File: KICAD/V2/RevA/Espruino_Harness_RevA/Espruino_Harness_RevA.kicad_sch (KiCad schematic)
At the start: 2 parts, among them J900 TARGET INTERFACE CONNECTOR A, J901 TARGET INTERFACE CONNECTOR B

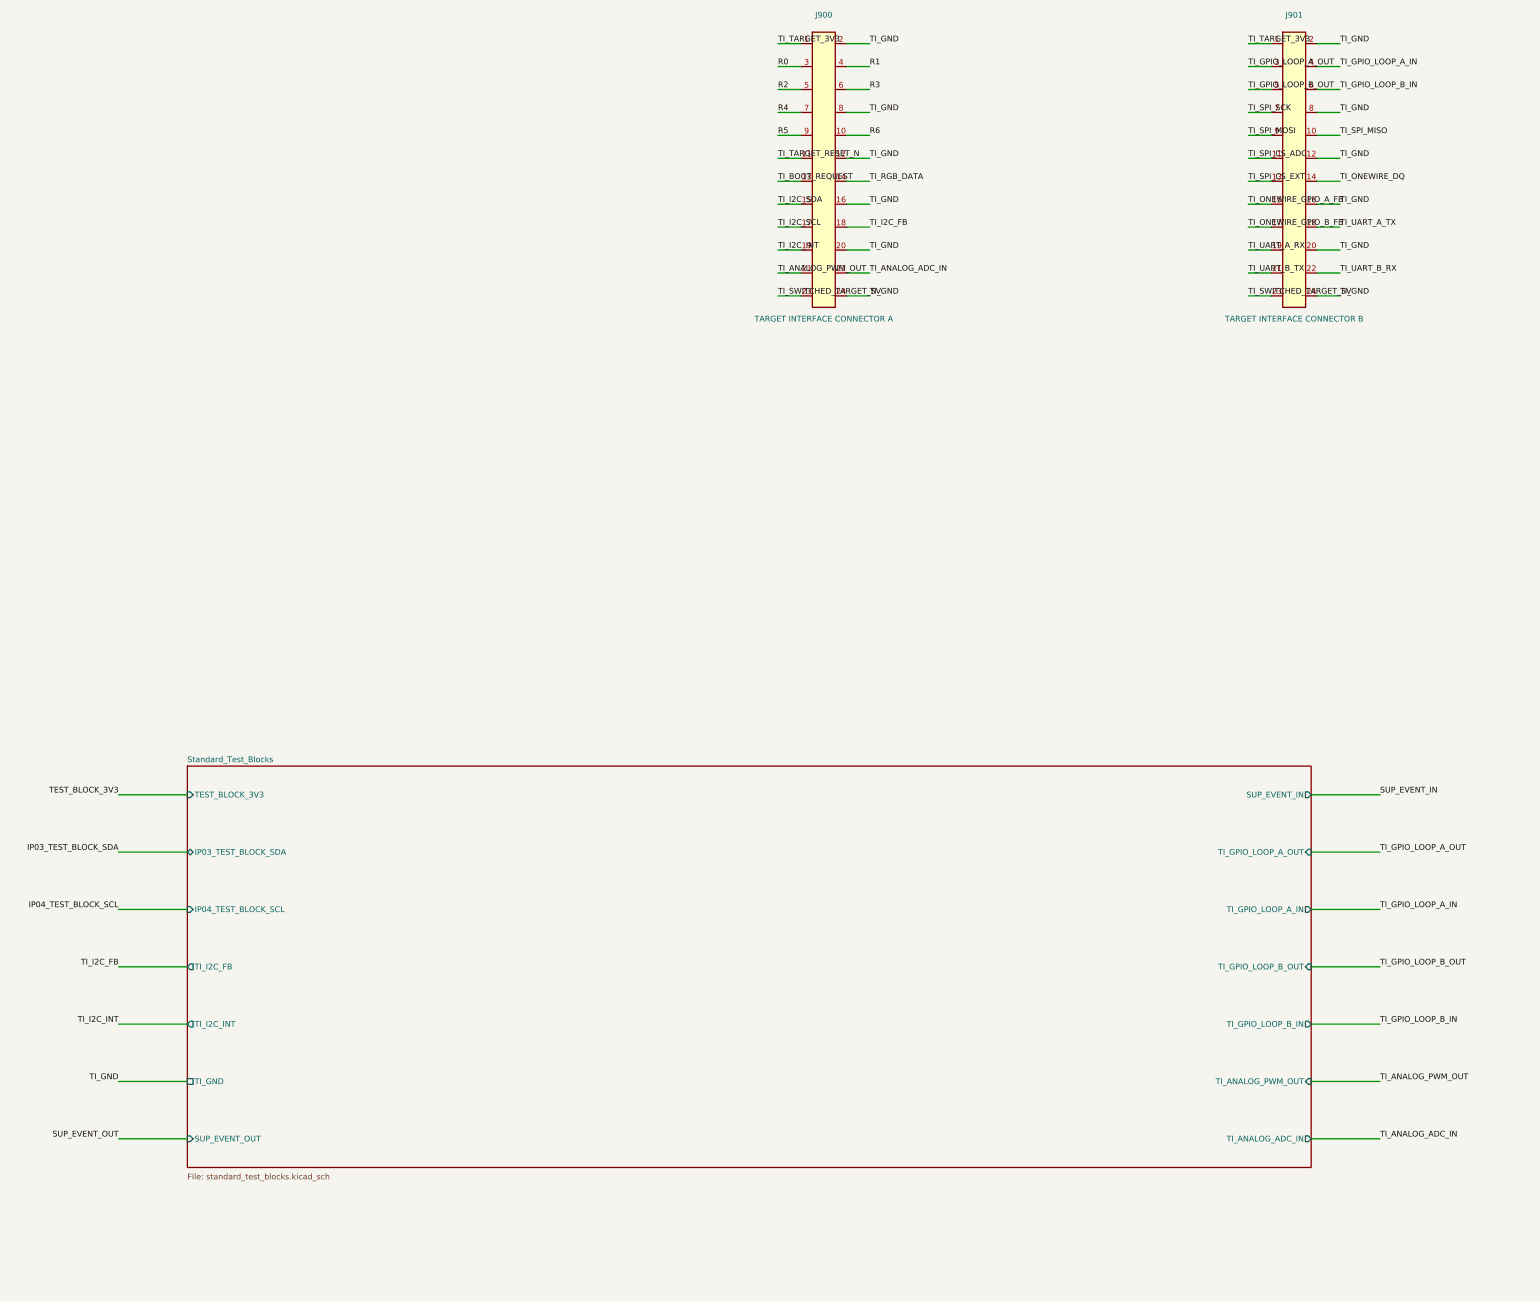
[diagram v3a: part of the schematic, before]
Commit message: Implement V2 SPI and 1-Wire test blocks
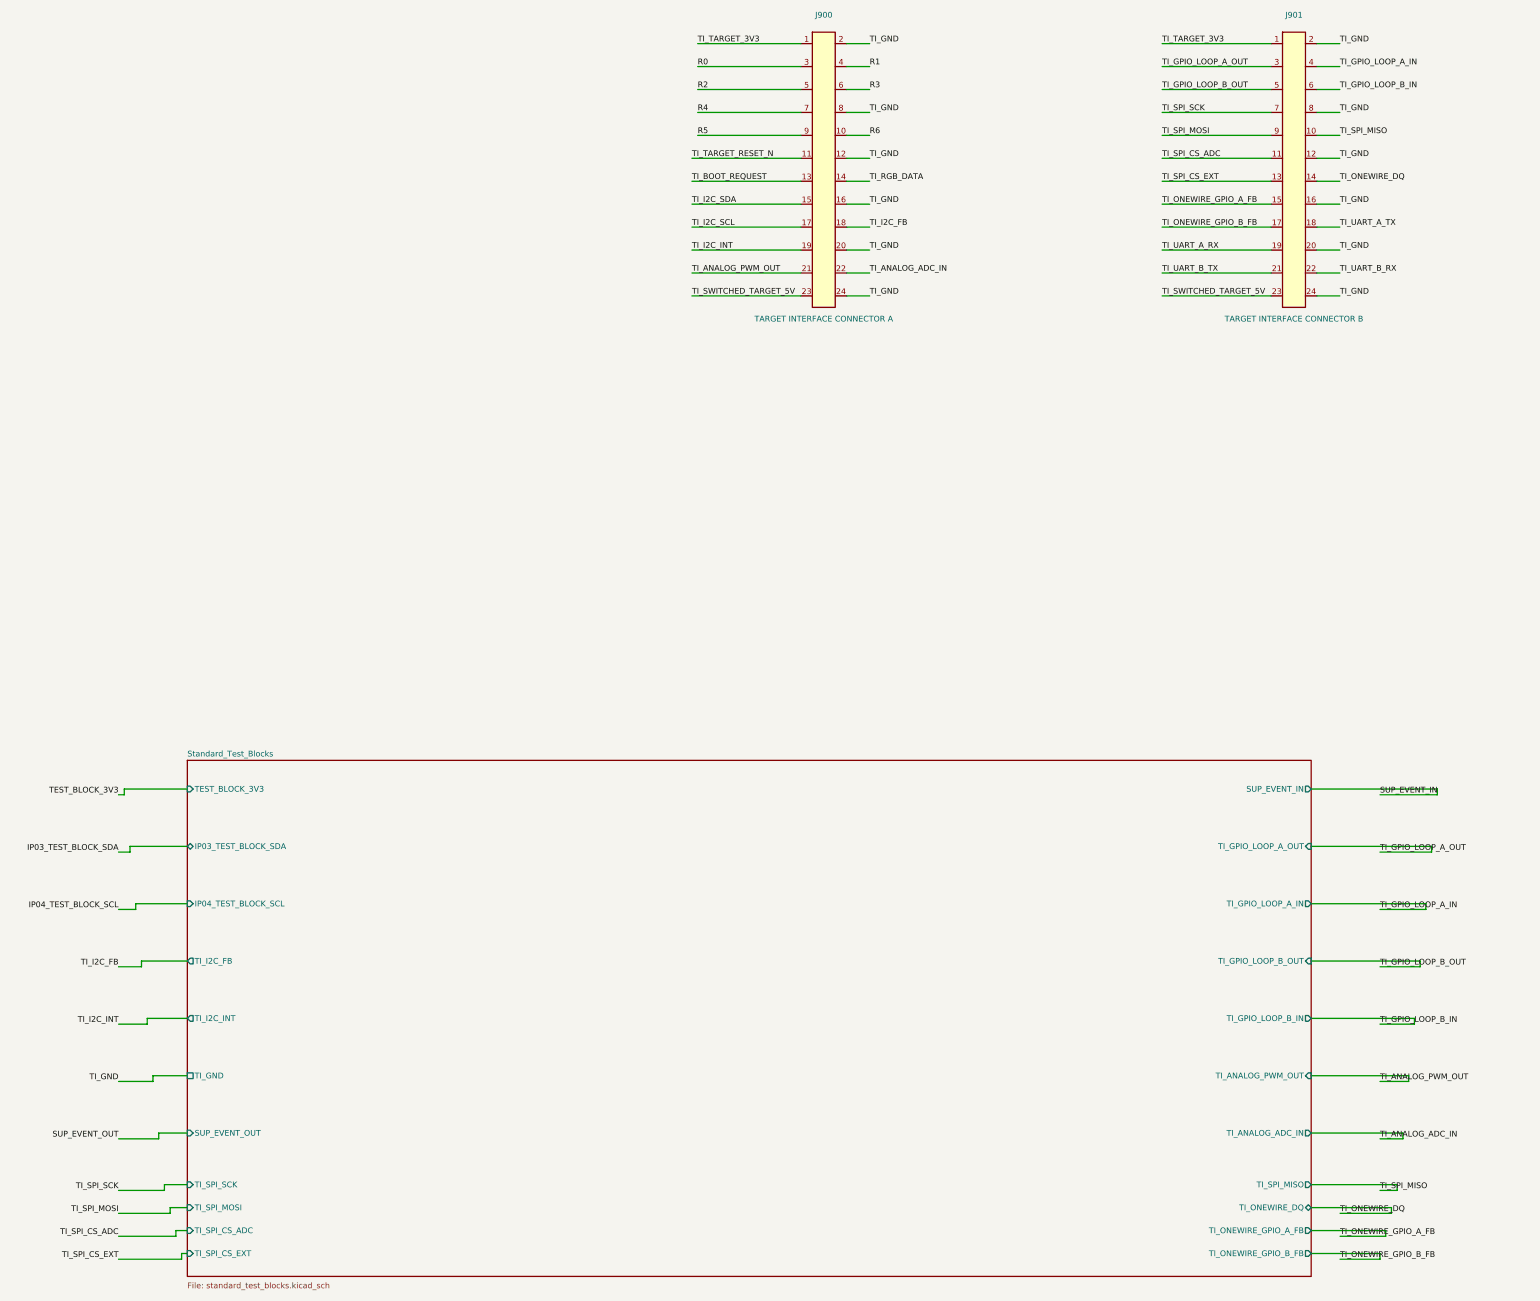
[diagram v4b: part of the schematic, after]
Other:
- sheet Standard_Test_Blocks ports: added TI_ONEWIRE_DQ, TI_ONEWIRE_GPIO_A_FB, TI_ONEWIRE_GPIO_B_FB, TI_SPI_CS_ADC, TI_SPI_CS_EXT, TI_SPI_MISO, TI_SPI_MOSI, TI_SPI_SCK; removed none

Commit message: Complete V2 standard test block schematic
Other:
- sheet Standard_Test_Blocks ports: added ROUTING_LOGIC_3V3, TI_RGB_DATA, TI_UART_A_RX, TI_UART_A_TX, TI_UART_B_RX, TI_UART_B_TX, UP01_EN, UP02_EN, UP03_EN, UP04_EN; removed none

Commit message: Implement V2 routing fabric and control
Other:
- added sheet Routing_Control (routing_control.kicad_sch)

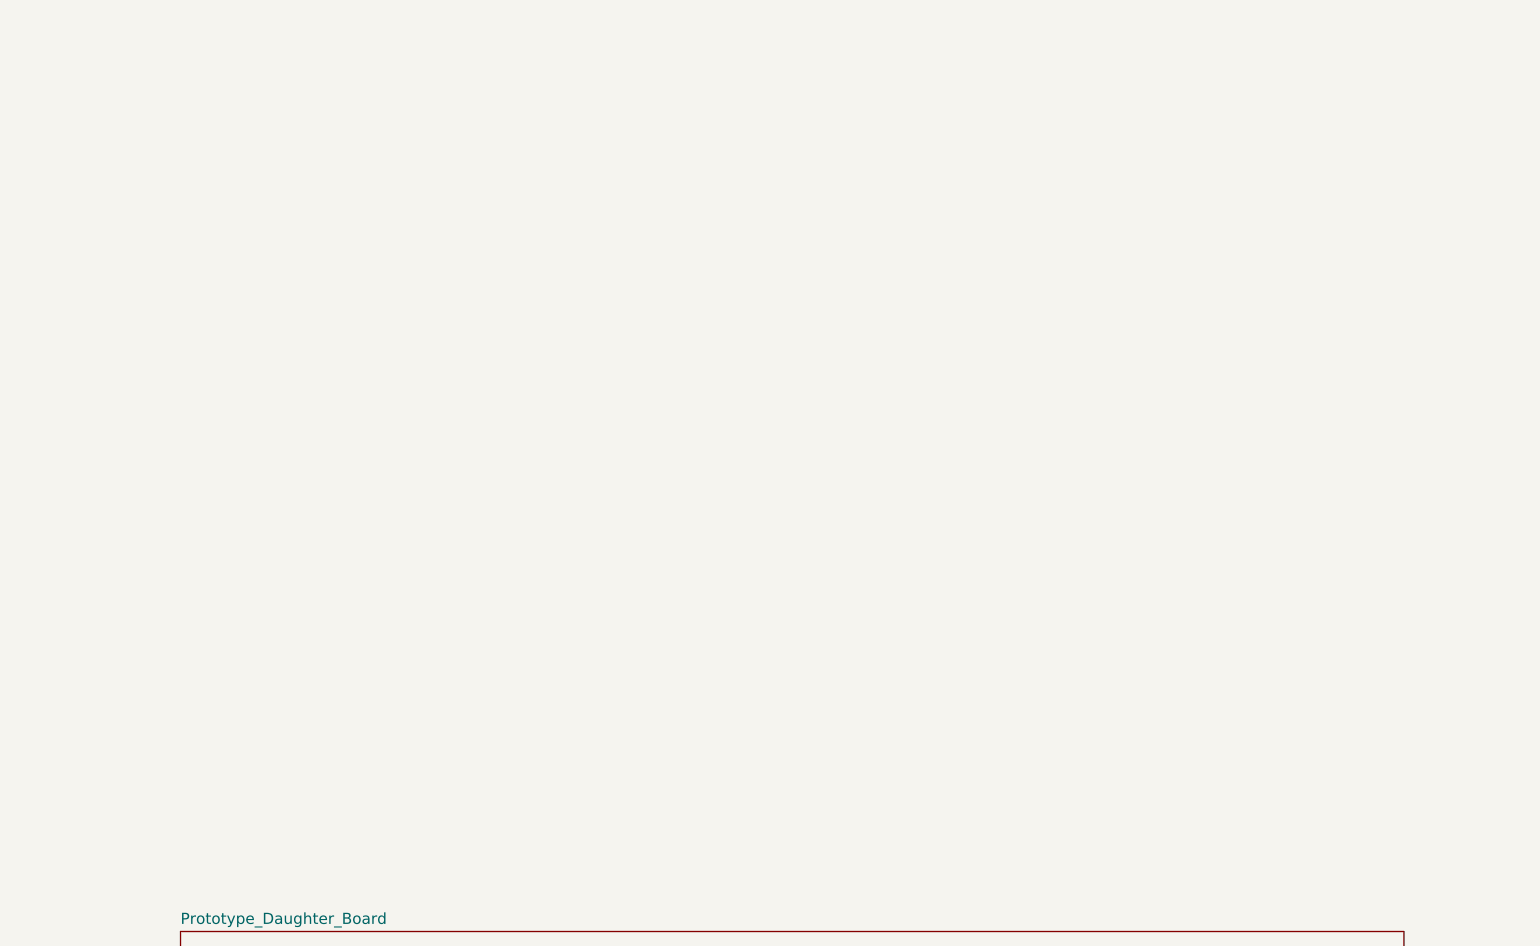
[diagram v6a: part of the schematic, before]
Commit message: Integrate Rev-A power control and rack supply requirements
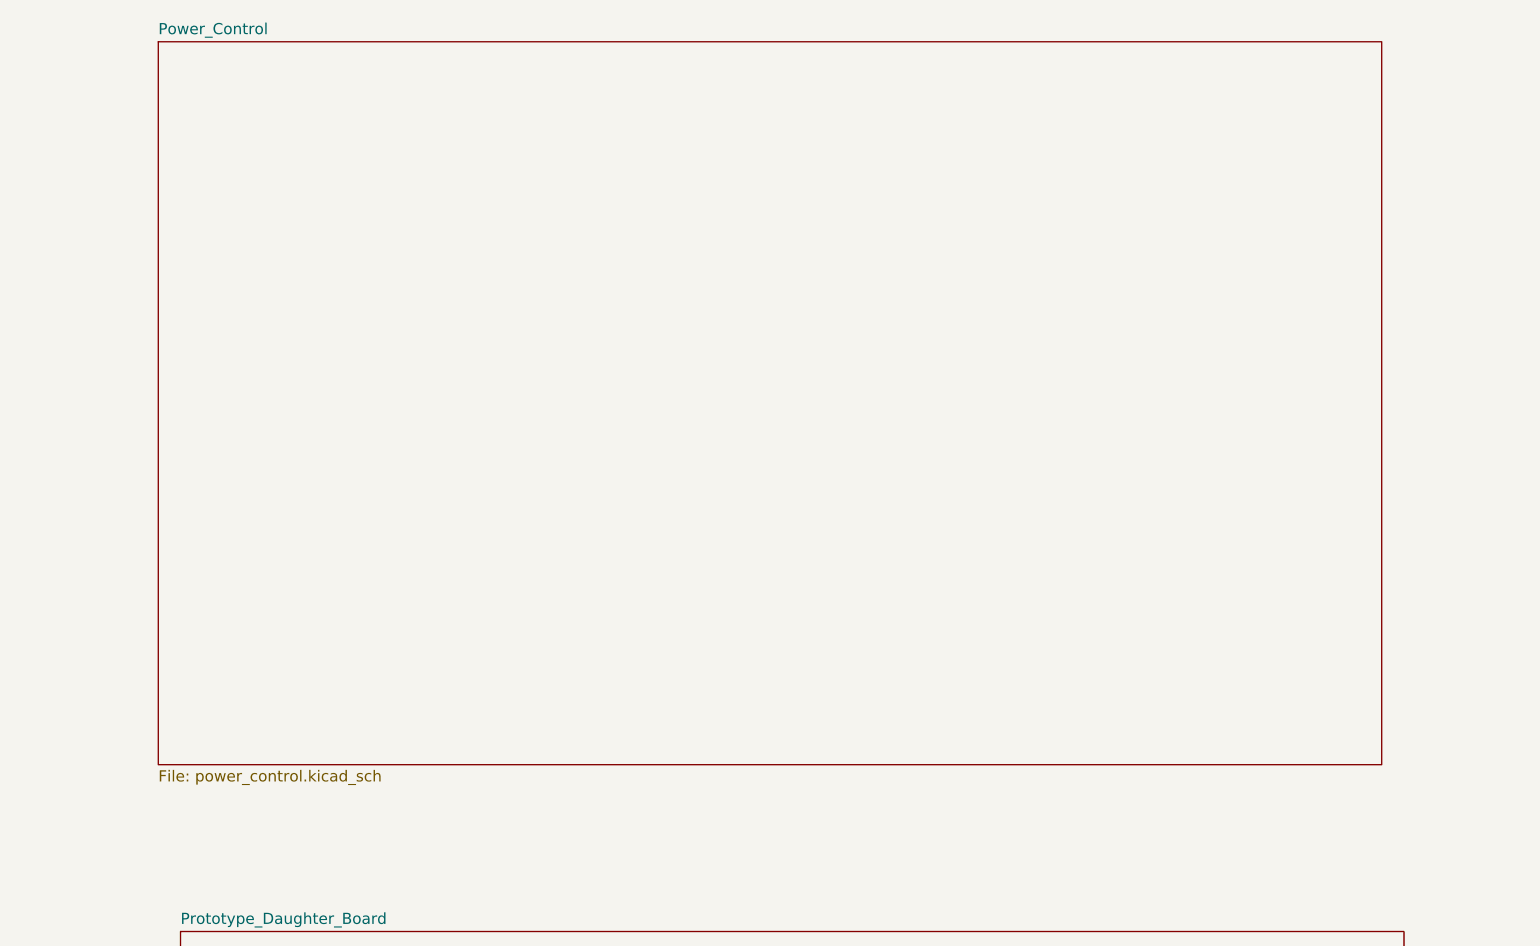
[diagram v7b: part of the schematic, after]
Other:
- added sheet Power_Control (power_control.kicad_sch)
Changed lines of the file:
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@@
+	)
+	(sheet
+		(at 421.64 22.86)
+		(size 139.7 82.55)
+		(exclude_from_sim no)
+		(in_bom yes)
+		(on_board yes)
+		(dnp no)
+		(fields_autoplaced yes)
+		(stroke
+			(width 0.1524)
+			(type solid)
+		)
+		(fill
+			(color 0 0 0 0.0000)
+		)
+		(property "Sheetname" "Power_Control"
+			(at 421.64 22.1484 0)
+			(effects
+				(font
+					(size 1.27 1.27)
+				)
+				(justify left bottom)
+			)
+		)
+		(property "Sheetfile" "power_control.kicad_sch"
+			(at 421.64 105.9946 0)
+			(effects
+				(font
+					(size 1.27 1.27)
+				)
+				(justify left top)
+			)
+		)
+		(instances
+			(project "Espruino_Harness_RevA"
+				(path "/12444148-a051-4fb0-ae7b-e3d34eecc954"
+					(page "5")
+				)
+			)
+		)
 	)
 	(sheet

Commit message: Establish Rev-A schematic verification framework
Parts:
- added J2: Grove_I2C_1x04, symbol Espruino_Harness_RevA:Grove_I2C_1x04
- added JBP1: RACK_POWER_BACKPLANE, Connector_PinHeader_2.54mm:PinHeader_2x06_P2.54mm_Vertical, symbol Connector_Generic:Conn_02x06_Odd_Even
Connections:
- net TI_GND: now also J2.4 (GND), JBP1.10 (Pin_10), JBP1.12 (Pin_12), JBP1.2 (Pin_2), JBP1.4 (Pin_4), JBP1.6 (Pin_6), JBP1.8 (Pin_8)
- new net EXT_3V3: JBP1.11 (Pin_11), JBP1.7 (Pin_7), JBP1.9 (Pin_9)
- new net EXT_5V: JBP1.1 (Pin_1), JBP1.3 (Pin_3), JBP1.5 (Pin_5)
- new net RACK_CONTROL_3V3: J2.3 (3V3)
- new net RACK_CONTROL_SCL: J2.1 (SCL)
- new net RACK_CONTROL_SDA: J2.2 (SDA)
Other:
- sheet Power_Control ports: added EXT_3V3, EXT_5V, RACK_CONTROL_3V3, RACK_CONTROL_SCL, RACK_CONTROL_SDA, ROUTING_LOGIC_3V3, TARGET_LOW_RANGE_EN, TARGET_POWER_ALERT_N, TARGET_POWER_EN, TARGET_POWER_FAULT_N, TEST_BLOCK_3V3, TEST_BLOCK_POWER_EN, TI_SWITCHED_TARGET_5V, TI_TARGET_3V3; removed none
- note added: "EXT_3V3 The external regulated 3.3 V supply entry TI_TARGET_3V3 Target Interface TI_TARGET_3V3 TEST_BLOCK_POWER_EN Rack Control Endpoint control output ROUTING_LOGIC_3V3 Matching inputs on Routing_Control and Standard_Test_Blocks TEST_BLOCK_3V3 Matching inputs on Routing_Control and Standard_Test_Blocks"
- note added: "Male 2x6 header for the Rev-A draft; three contacts per supply with adjacent returns"
- note added: "RACK POWER BACKPLANE INTERFACE - PROVISIONAL"
- note added: "Rack Backplane Interface"
- note added: "Rack Control Grove interface"
- note added: "Rev-A Reusable Harness Board"
- note added: "Target Interface pin banks"
- company: ESP32_SGATest -> SimonGAndrews
- title: V2 Rev-A Reusable Harness - System, Control and Routing -> V2 Rev-A Reusable Harness Board 
- moved on the sheet: J900, J901
